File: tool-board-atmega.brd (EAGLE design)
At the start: 112 x 104 mm, 84 parts, among them IC3 ATMEGA2560-16AU, IC4 ATMEGA8U2-MU, Q1 16MHz, X2 MICROUSB_VERTICAL, Y2 16MHz

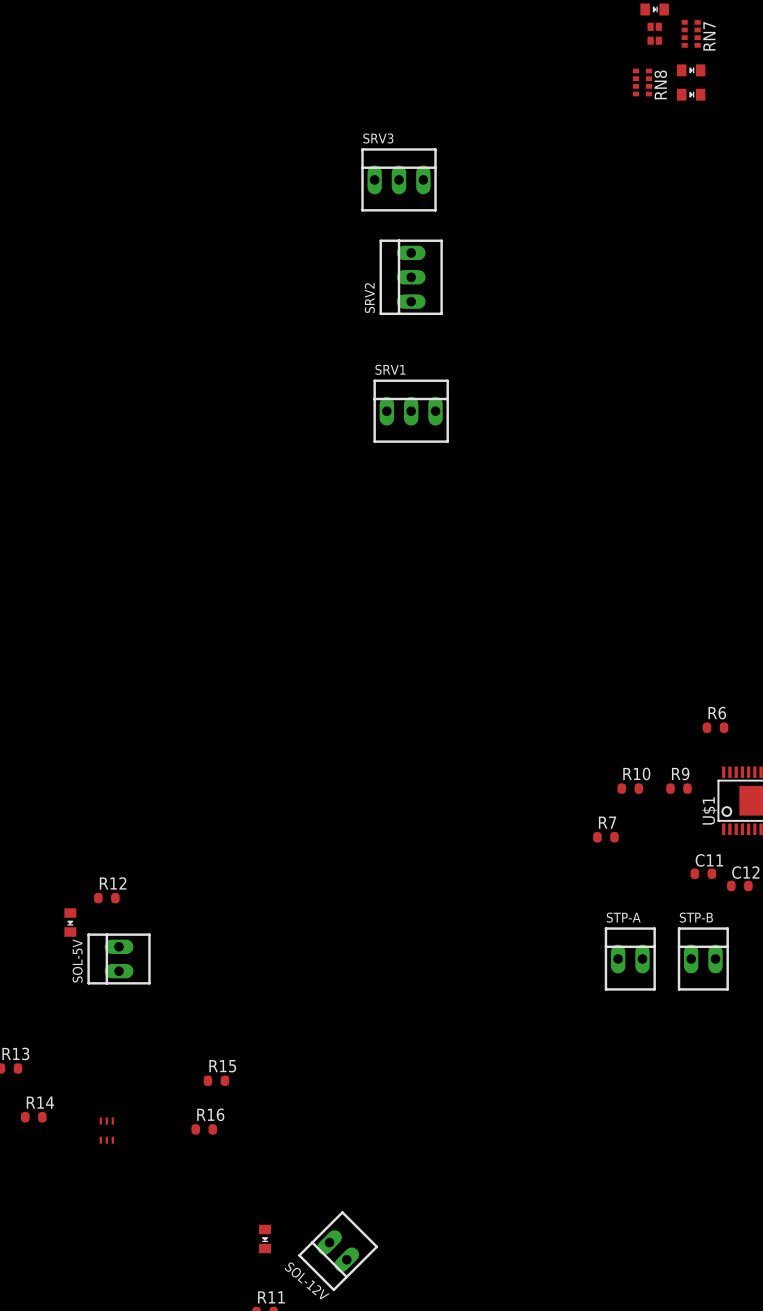
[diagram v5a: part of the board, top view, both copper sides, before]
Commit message: changed LEDs and Diodes to all be 0603 package
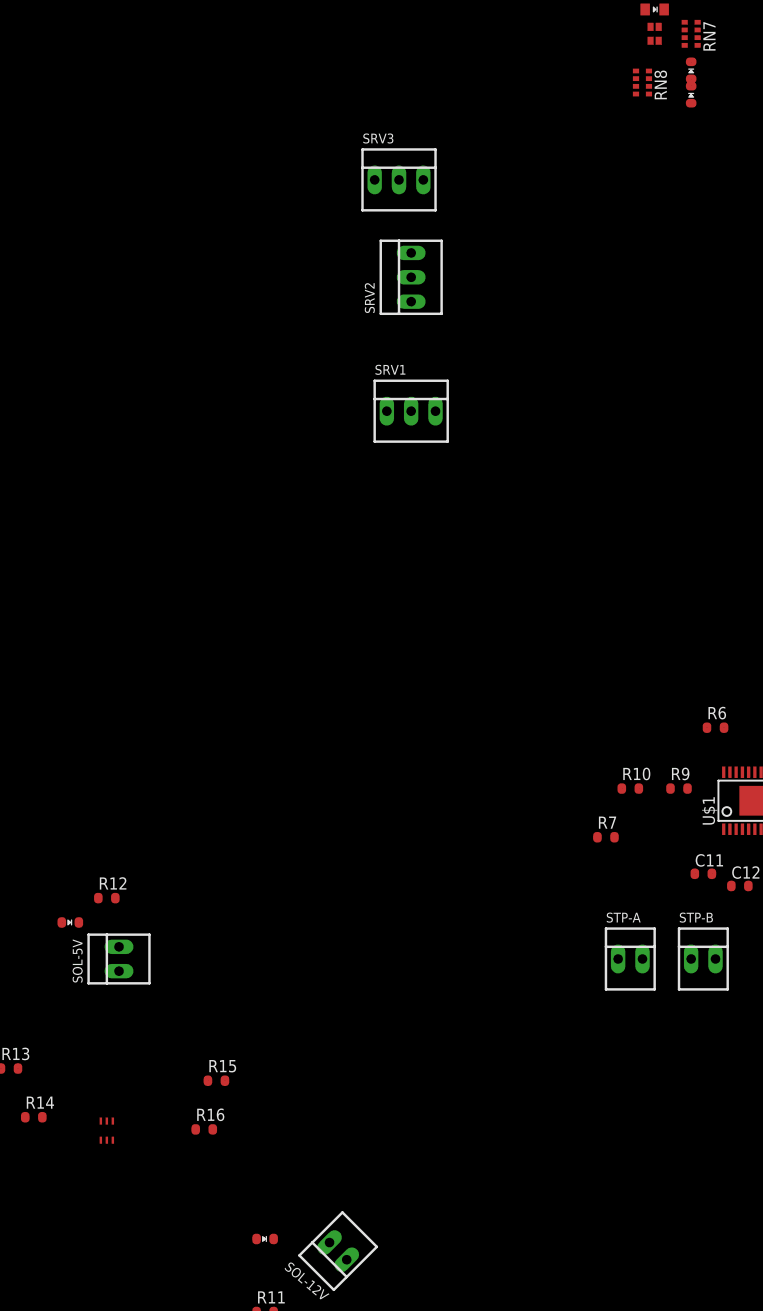
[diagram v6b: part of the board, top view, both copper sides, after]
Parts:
- R15: device SmartPrj:R0603-ROUND -> tool-board-atmega:SMARTPRJ_R0603-ROUND
- U$16, U$17: value DIODE0805 -> 0603DIODE; device ClinicalRobotics:0805LED -> ClinicalRobotics:SMARTPRJ_C0603-ROUND
- U$20, U$21: value 0805LED -> 0603LED; device ClinicalRobotics:0805LED -> ClinicalRobotics:SMARTPRJ_C0603-ROUND
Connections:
- net N$17: now also U$16.1; no longer U$16.P$1
- net N$18: now also U$17.1; no longer U$17.P$1
- net N$19: now also U$16.2; no longer U$16.P$2
- net N$21: now also U$17.2; no longer U$17.P$2
- net N$28: now also U$21.2; no longer U$21.P$2
- net N$29: now also U$20.2; no longer U$20.P$2
- net N$30: now also U$20.1; no longer U$20.P$1
- net N$31: now also U$21.1; no longer U$21.P$1
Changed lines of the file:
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@@
 <element name="U$13" library="ClinicalRobotics" package="SPRING_CONTACT" value="SPRING_CONTACT" x="-20.701" y="-44.45" smashed="yes"/>
 <element name="U$15" library="ClinicalRobotics" package="SC-88" value="DUALNMOS-SSM6N7002KFULFCT" x="-194.31" y="-45.72" smashed="yes"/>
-<element name="U$16" library="ClinicalRobotics" package="0805LED" value="DIODE0805" x="-177.8" y="-57.15" smashed="yes"/>
-<element name="U$17" library="ClinicalRobotics" package="0805LED" value="DIODE0805" x="-198.12" y="-24.13" smashed="yes"/>
+<element name="U$16" library="ClinicalRobotics" package="SMARTPRJ_C0603-ROUND" value="0603DIODE" x="-177.8" y="-57.15" smashed="yes"/>
+<element name="U$17" library="ClinicalRobotics" package="SMARTPRJ_C0603-ROUND" value="0603DIODE" x="-198.12" y="-24.13" smashed="yes"/>
 <element name="U$18" library="ClinicalRobotics" package="RGBLED" value="RGBLED" x="-137.16" y="68.58" smashed="yes" rot="R180"/>
 <element name="U$19" library="ClinicalRobotics" package="0805LED" value="0805LED" x="-137.16" y="71.12" smashed="yes" rot="R90"/>
 <element name="U$2" library="SmartPrj" package="FIDUCIA-MOUNT" value="FIDUCIALMOUNT" x="-227.33" y="33.02" smashed="yes"/>
-<element name="U$20" library="ClinicalRobotics" package="0805LED" value="0805LED" x="-133.35" y="64.77" smashed="yes" rot="R90"/>
-<element name="U$21" library="ClinicalRobotics" package="0805LED" value="0805LED" x="-133.35" y="62.23" smashed="yes" rot="R90"/>
+<element name="U$20" library="ClinicalRobotics" package="SMARTPRJ_C0603-ROUND" value="0603LED" x="-133.35" y="64.77" smashed="yes" rot="R90"/>
+<element name="U$21" library="ClinicalRobotics" package="SMARTPRJ_C0603-ROUND" value="0603LED" x="-133.35" y="62.23" smashed="yes" rot="R90"/>
 <element name="U$3" library="SmartPrj" package="FIDUCIA-MOUNT" value="FIDUCIALMOUNT" x="-231.14" y="33.02" smashed="yes"/>
 <element name="U$4" library="SmartPrj" package="FIDUCIA-MOUNT" value="FIDUCIALMOUNT" x="-234.95" y="33.02" smashed="yes"/>
@@
 <attribute name="VALUE" x="-202.819" y="-46.482" size="1.27" layer="27"/>
 </element>
-<element name="R15" library="SmartPrj" package="R0603-ROUND" value="1M" x="-182.88" y="-40.64" smashed="yes">
+<element name="R15" library="tool-board-atmega" package="SMARTPRJ_R0603-ROUND" value="1M" x="-182.88" y="-40.64" smashed="yes">
 <attribute name="NAME" x="-183.769" y="-39.751" size="1.27" layer="25"/>
 <attribute name="VALUE" x="-183.769" y="-42.672" size="1.27" layer="27"/>
@@
 <contactref element="U$15" pad="P$3"/>
 <contactref element="SOL-12V" pad="2"/>
-<contactref element="U$16" pad="P$1"/>
-<wire x1="-177.8" y1="-56.1594" x2="-193.685" y2="-46.845" width="0" layer="19" extent="1-1"/>
-<wire x1="-171.078028125" y1="-57.521975" x2="-177.8" y2="-56.1594" width="0" layer="19" extent="1-1"/>
+<contactref element="U$16" pad="1"/>
+<wire x1="-178.689" y1="-57.15" x2="-193.685" y2="-46.845" width="0" layer="19" extent="1-1"/>
+<wire x1="-171.078028125" y1="-57.521975" x2="-178.689" y2="-57.15" width="0" layer="19" extent="1-1"/>
 </signal>
 <signal name="N$18">
 <contactref element="U$15" pad="P$6"/>
 <contactref element="SOL-5V" pad="2"/>
-<contactref element="U$17" pad="P$1"/>
+<contactref element="U$17" pad="1"/>
 <wire x1="-193.04" y1="-26.67" x2="-194.935" y2="-44.845" width="0" layer="19" extent="1-1"/>
-<wire x1="-198.12" y1="-23.1394" x2="-193.04" y2="-26.67" width="0" layer="19" extent="1-1"/>
+<wire x1="-199.009" y1="-24.13" x2="-193.04" y2="-26.67" width="0" layer="19" extent="1-1"/>
 </signal>
 <signal name="N$19">
 <contactref element="SOL-12V" pad="1"/>
 <contactref element="R11" pad="1"/>
-<contactref element="U$16" pad="P$2"/>
-<wire x1="-177.8" y1="-58.1406" x2="-178.689" y2="-64.77" width="0" layer="19" extent="1-1"/>
-<wire x1="-169.281975" y1="-59.318028125" x2="-177.8" y2="-58.1406" width="0" layer="19" extent="1-1"/>
+<contactref element="U$16" pad="2"/>
+<wire x1="-176.911" y1="-57.15" x2="-178.689" y2="-64.77" width="0" layer="19" extent="1-1"/>
+<wire x1="-169.281975" y1="-59.318028125" x2="-176.911" y2="-57.15" width="0" layer="19" extent="1-1"/>
 </signal>
 <signal name="N$21">
 <contactref element="SOL-5V" pad="1"/>
 <contactref element="R12" pad="1"/>
-<contactref element="U$17" pad="P$2"/>
-<wire x1="-198.12" y1="-25.1206" x2="-193.04" y2="-29.21" width="0" layer="19" extent="1-1"/>
-<wire x1="-195.199" y1="-21.59" x2="-198.12" y2="-25.1206" width="0" layer="19" extent="1-1"/>
+<contactref element="U$17" pad="2"/>
+<wire x1="-197.231" y1="-24.13" x2="-193.04" y2="-29.21" width="0" layer="19" extent="1-1"/>
+<wire x1="-195.199" y1="-21.59" x2="-197.231" y2="-24.13" width="0" layer="19" extent="1-1"/>
 </signal>
 <signal name="N$20">
@@
 </signal>
 <signal name="N$28">
-<contactref element="U$21" pad="P$2"/>
+<contactref element="U$21" pad="2"/>
 <contactref element="IC3" pad="9"/>
-<wire x1="-90.55" y1="26.13" x2="-132.3594" y2="62.23" width="0" layer="19" extent="1-1"/>
+<wire x1="-90.55" y1="26.13" x2="-133.35" y2="63.119" width="0" layer="19" extent="1-1"/>
 </signal>
 <signal name="N$29">
 <contactref element="IC3" pad="8"/>
-<contactref element="U$20" pad="P$2"/>
-<wire x1="-90.55" y1="26.63" x2="-132.3594" y2="64.77" width="0" layer="19" extent="1-1"/>
+<contactref element="U$20" pad="2"/>
+<wire x1="-90.55" y1="26.63" x2="-133.35" y2="65.659" width="0" layer="19" extent="1-1"/>
 </signal>
 <signal name="N$30">
-<contactref element="U$20" pad="P$1"/>
+<contactref element="U$20" pad="1"/>
 <contactref element="RN8" pad="4"/>
-<wire x1="-134.3406" y1="64.77" x2="-137.755" y2="64.7" width="0" layer="19" extent="1-1"/>
+<wire x1="-133.35" y1="63.881" x2="-137.755" y2="64.7" width="0" layer="19" extent="1-1"/>
 </signal>
 <signal name="N$31">
 <contactref element="RN8" pad="3"/>
-<contactref element="U$21" pad="P$1"/>
-<wire x1="-134.3406" y1="62.23" x2="-137.755" y2="63.9" width="0" layer="19" extent="1-1"/>
+<contactref element="U$21" pad="1"/>
+<wire x1="-133.35" y1="61.341" x2="-137.755" y2="63.9" width="0" layer="19" extent="1-1"/>
 </signal>
 <signal name="N$32">

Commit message: placed all components, made Servo connectors 4 pin
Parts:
- removed SRV1, SRV2, SRV3: 22-23-2031, con-molex:22-23-2031
- added X1, X3, X4: 22-23-2041, con-molex:22-23-2041
- moved R14 250.7 mm to (46.1, -8.00), turned to 270 degrees
- moved R13 250.4 mm to (43.9, -8.00), turned to 90 degrees
- moved U$15 242.6 mm to (44.5, -2.54)
- moved R12 238.7 mm to (44.3, -16.1)
- moved R16 234.4 mm to (45.3, 1.78), turned to 90 degrees
- moved SOL-5V 230.7 mm to (36.8, -8.89)
- moved U$17 230.5 mm to (31.9, -8.76), turned to 270 degrees
- moved R15 230.0 mm to (43.2, 1.78), turned to 90 degrees
- moved R11 226.6 mm to (44.3, -19.8)
- moved U$16 212.9 mm to (32.0, -21.2), turned to 270 degrees
- moved SOL-12V 211.0 mm to (36.8, -17.8), turned to 90 degrees
- moved UBOOT 106.5 mm to (-58.5, -5.97)
- moved Z4 103.1 mm to (-51.7, -9.91), flipped to the bottom, turned to 270 degrees
- moved R7 102.2 mm to (-40.6, -3.81), flipped to the bottom, turned to 180 degrees
- moved R10 102.1 mm to (-39.4, 8.89), turned to 180 degrees
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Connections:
- new net PA4: IC3.74
- new net PA5: IC3.73, X4.4
- new net PA6: IC3.72, X3.4
- new net PA7: IC3.71, X1.4
- net +5V: now also U$19.P$1, X1.2, X3.2, X4.2; no longer SRV1.2, SRV2.2, SRV3.2
- net GND: now also X1.1, X3.1, X4.1; no longer SRV1.1, SRV2.1, SRV3.1
- net PB5: now also X4.3
- net PB6: now also X3.3
- net PB7: now also X1.3
- net PE3: no longer SRV1.3
- net PE4: no longer SRV2.3
- net PE5: no longer SRV3.3
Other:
- board size 112 x 104 mm -> 144 x 104 mm

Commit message: polys poured, local power vias placed
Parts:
- added C14: 100uF, rcl:E3,5-8
- added U$6: SPRING_CONTACT, ClinicalRobotics:SPRING_CONTACT
- moved STP-B 7.43 mm to (-28.0, -35.4), turned to 325 degrees
- moved STP-A 4.50 mm to (-33.6, -31.8), turned to 325 degrees
- moved U$10 1.05 mm to (0.00, -49.0)
- moved U$16 0.56 mm to (32.3, -21.7)
- moved C13 0.50 mm to (-31.8, 6.85)
- moved R8 0.45 mm to (-32.1, 1.02)
- moved RN8 0.25 mm to (-48.3, 39.1)
- moved U$20 0.25 mm to (-59.7, 39.1)
- moved U$21 0.25 mm to (-57.1, 39.1)
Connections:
- new net +24V: C14.+, U$6.P$1
- net +12V: now also U$12.P$1
- net +12VIN: no longer U$12.P$1
- net GND: now also C14.-, U$11.P$1
- net UGND: no longer U$11.P$1
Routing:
- net GND: track 0.00 -> 77.4 mm, vias 0 -> 36
- net +5V: track 0.00 -> 1.09 mm, vias 0 -> 1
- added copper zone on layer 1, net +5V
- added copper zone on layer 16, net GND
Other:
- outline, holes or cut-outs redrawn
